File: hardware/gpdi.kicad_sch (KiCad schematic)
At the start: 9 parts, among them J1 GPDI_A, Q1 BSN20

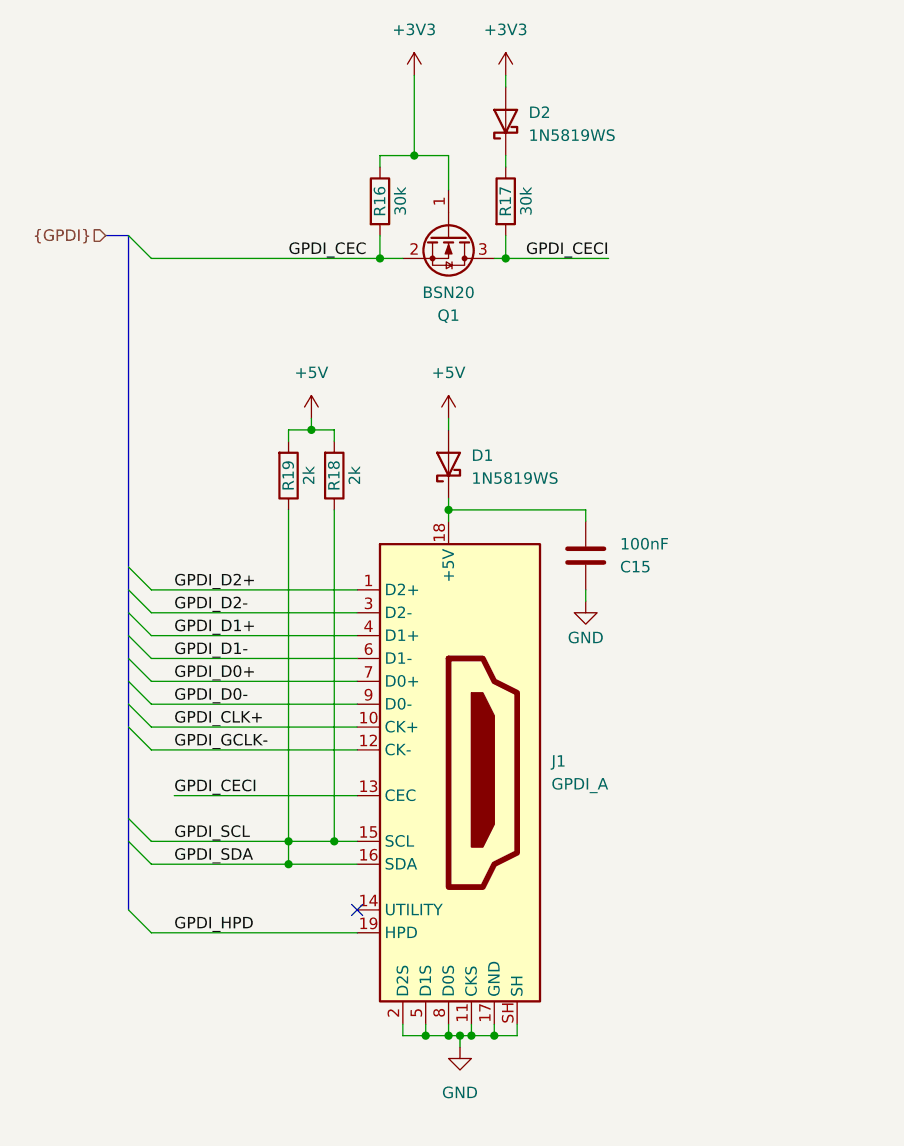
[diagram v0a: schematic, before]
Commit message: Added TVS diodes, RF switch and changed RJ45 conn
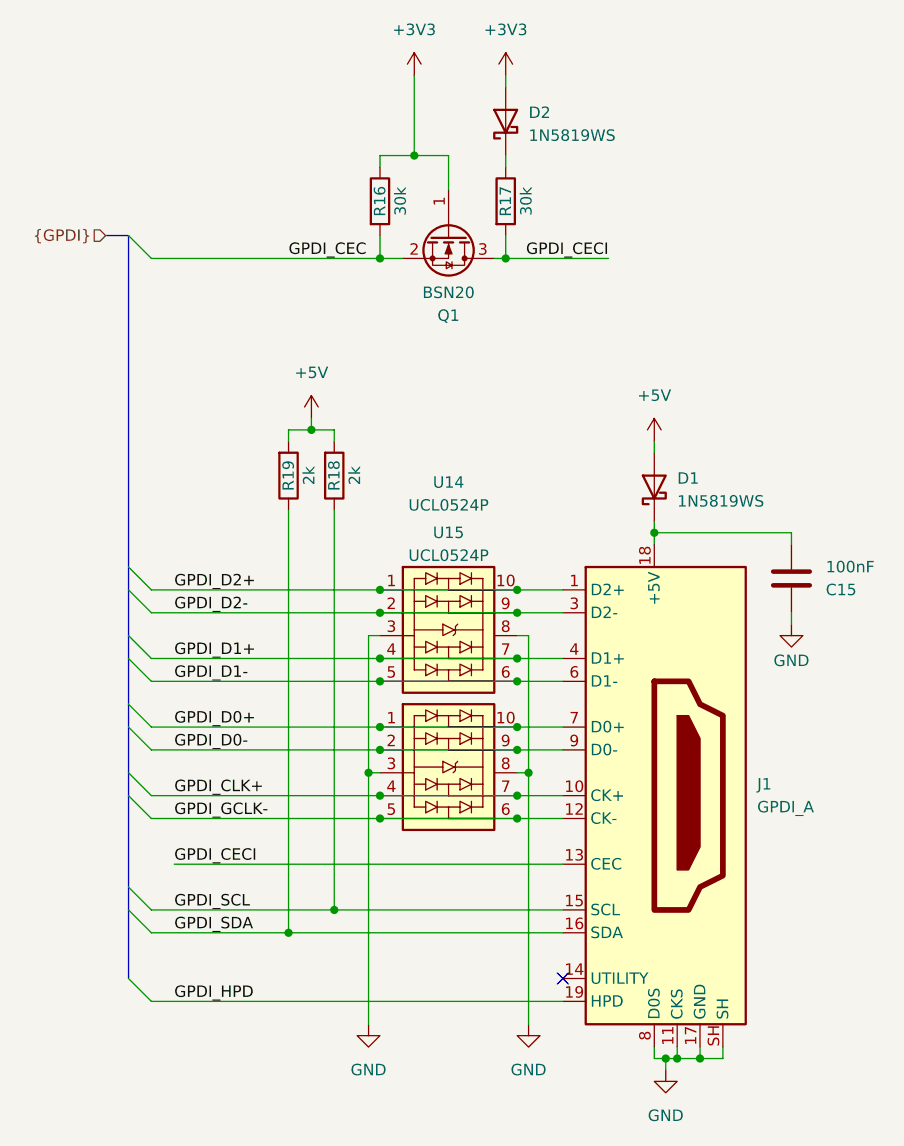
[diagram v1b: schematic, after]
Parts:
- added U14, U15: UCL0524P, Package_DFN_QFN:Diodes_UDFN-10_1.0x2.5mm_P0.5mm, symbol cm0:UCL0524P
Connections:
- net GPDI_CLK+: now also U15.4, U15.7
- net GPDI_D0+: now also U15.1, U15.10
- net GPDI_D0-: now also U15.2, U15.9
- net GPDI_D1+: now also U14.4, U14.7
- net GPDI_D1-: now also U14.5, U14.6
- net GPDI_D2+: now also U14.1, U14.10
- net GPDI_D2-: now also U14.2, U14.9
- net GPDI_GCLK-: now also U15.5, U15.6
- net GPDI_SCL: no longer J1.16 (SDA), R19.1
- net GND renamed D1S
- net D1S: now also U14.3, U14.8, U15.3, U15.8
- new net GPDI_SDA: J1.16 (SDA), R19.1
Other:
- moved on the sheet: C15, D1
